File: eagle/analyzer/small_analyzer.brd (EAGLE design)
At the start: 55.5 x 30.5 mm, 22 parts, among them IC1 MCP604ST, IC2 TPS77301, IC3 MSP430FW42IP, U1 AD5933

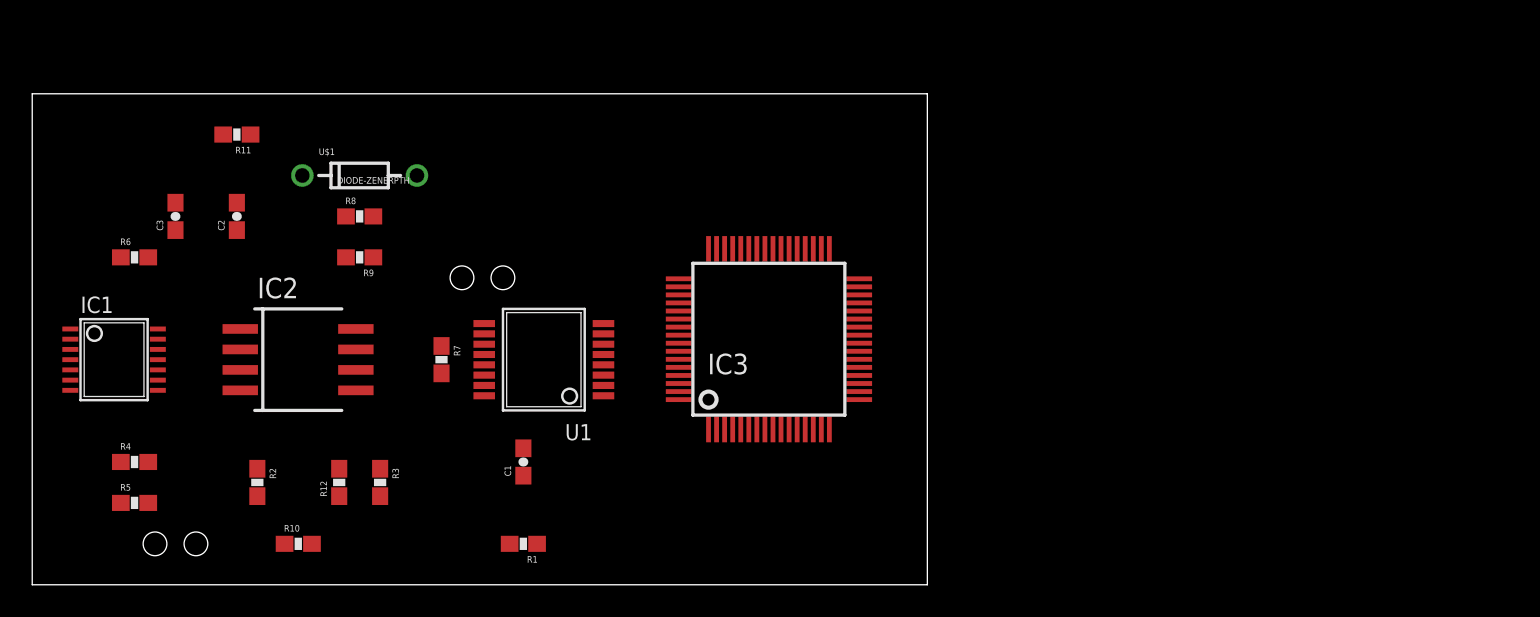
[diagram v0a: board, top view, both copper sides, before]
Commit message: added ground planes, expanded board, changed mcu to atmega328
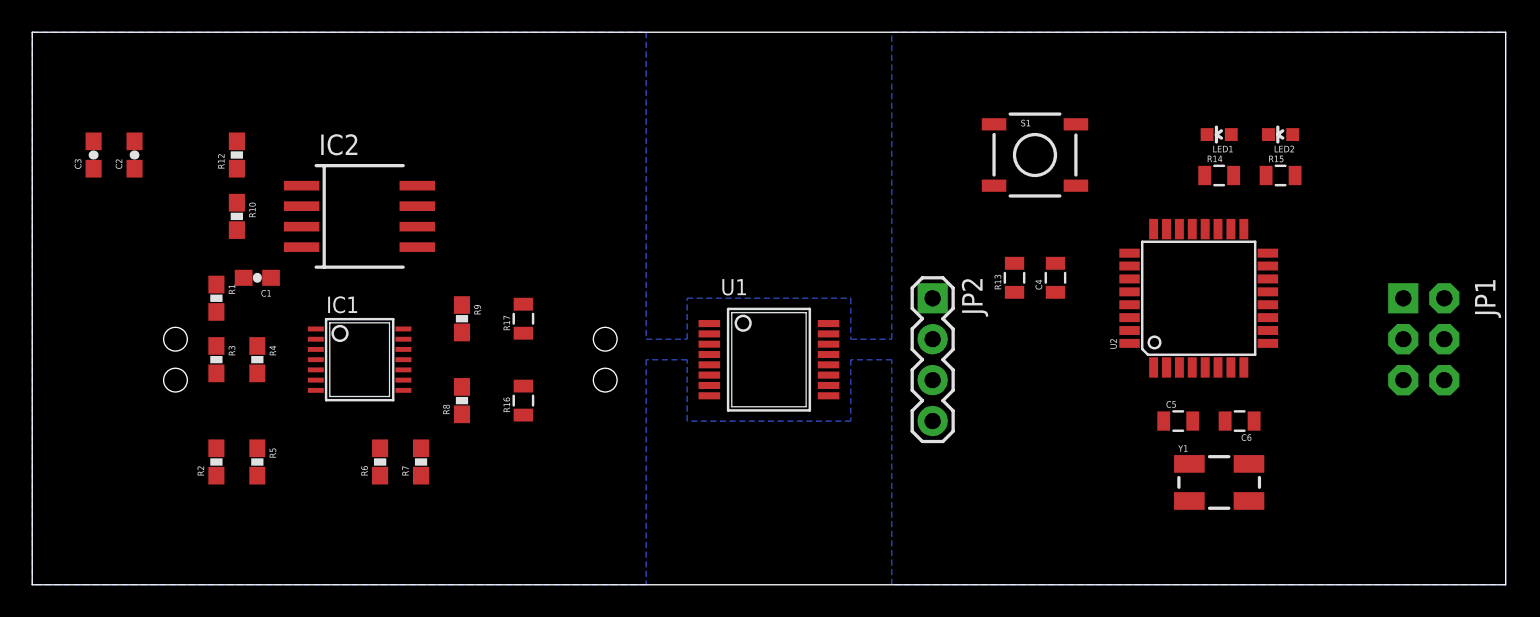
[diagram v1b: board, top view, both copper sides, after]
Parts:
- removed IC3: MSP430FW42IP, texas:SQFP-S-10X10-64
- removed R11: 10k, SparkFun-Passives:0603-RES
- removed U$1: DIODE-ZENERPTH, SparkFun-DiscreteSemi:DIODE-ZENER
- added C4: 0.1uF, SparkFun-Passives:0805
- added C5, C6: 22pF, SparkFun-Passives:0805
- added JP1: (no value), SparkFun-Connectors:2X3-NS
- added JP2: (no value), SparkFun-Connectors:1X04
- added LED1, LED2: (no value), SparkFun-LED:LED-0603
- added R13: 10k, SparkFun-Passives:0805
- added R14, R15: 4.7k, SparkFun-Passives:0805
- added R16, R17: 100k, SparkFun-Passives:0805
- added S1: (no value), SparkFun-Electromechanical:TACTILE_SWITCH_SMD
- added U2: ATMEGA328P, SparkFun-DigitalIC:TQFP32-08
- added Y1: (no value), SparkFun-FreqCtrl:CRYSTAL-SMD-5X3
- moved R1 24.4 mm to (11.4, 17.8), turned to 270 degrees
- moved R12 21.3 mm to (12.7, 26.7)
- moved R10 20.7 mm to (12.7, 22.9), turned to 270 degrees
- moved C1 20.1 mm to (14.0, 19.1), turned to 180 degrees
- moved R6 19.8 mm to (21.6, 7.62), turned to 90 degrees
- moved IC1 15.2 mm to (20.3, 14.0)
- moved U1 14.0 mm to (45.7, 14.0), turned to 270 degrees
- moved R8 13.1 mm to (26.7, 11.4), turned to 90 degrees
- moved LOAD 12.8 mm to (8.89, 15.2), turned to 270 degrees
- moved R3 12.7 mm to (11.4, 14.0)
- moved RFB 10.9 mm to (35.6, 12.7), turned to 90 degrees
- moved R4 9.92 mm to (14.0, 14.0), turned to 270 degrees
- moved IC2 9.67 mm to (20.3, 22.9)
- moved R5 8.03 mm to (14.0, 7.62), turned to 270 degrees
- moved C2 7.41 mm to (6.35, 26.7)
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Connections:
- removed net AVCC: IC3.64
- removed net AVSS: IC3.62
- removed net DVCC: IC3.1
- removed net DVSS: IC3.63
- new net CS: U2.14
- new net MISO: JP1.1, U2.16
- new net MOSI: JP1.4, U2.15
- new net N$10: LED2.A, R15.2
- new net N$11: C4.2, R13.1, S1.3, S1.4, U2.29
- new net N$12: LED1.A, R14.2
- new net N$15: IC1.12, R16.2, R17.1
- new net N$17: U2.23
- new net N$4: C5.2, U2.7, Y1.1
- new net N$9: C6.2, U2.8, Y1.3
- new net RST: C4.1, JP1.5
- new net SCK: JP1.3, R15.1, U2.17
- net GND: now also C5.1, C6.1, JP1.6, JP2.4, LED1.C, LED2.C, R16.1, S1.1, S1.2, U2.21, U2.3, U2.5; no longer U$1.P$2
- net MCLK: now also JP2.3
- net SCL: now also JP2.1, U2.28
- net SDA: now also JP2.2, U2.27
- net VCC: now also JP1.2, R13.2, R14.1, R17.2, U2.18, U2.20, U2.4, U2.6; no longer R11.2
- net VREF: now also IC1.13, IC1.14; no longer R11.1, U$1.P$1
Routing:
- added copper zone on layer 16, net GND
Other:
- board size 55.5 x 30.5 mm -> 91.4 x 34.3 mm

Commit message: updated
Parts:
- removed C3: 0.1uF, SparkFun-Passives:0603-CAP
- removed LOAD, RFB: M02POGO_PIN_HOLES_ONLY, SparkFun-Connectors:1X02_PP_HOLES_ONLY
- added C7: 10uF, SparkFun-Passives:0603-CAP
- added C8: 0.1uF, SparkFun-Passives:0603-CAP
- added IC3: TPS77350, texas:SOP-08
- added JP3: (no value), SparkFun-Connectors:1X04
- added JP4: (no value), SparkFun-Connectors:1X06_LOCK
- C2: value 10uF -> 0.1uF
- moved C2 36.3 mm to (35.6, 5.08), turned to 270 degrees
- moved JP2 13.0 mm to (53.3, 30.5)
- moved U1 11.7 mm to (43.2, 25.4)
- moved JP1 3.59 mm to (83.8, 17.8)
- moved C5 3.59 mm to (68.6, 12.7)
- moved C6 3.59 mm to (72.4, 12.7)
- moved U2 3.59 mm to (69.8, 20.3)
- moved C4 3.59 mm to (61.0, 21.6)
- moved R13 3.59 mm to (58.4, 21.6)
- moved S1 3.59 mm to (59.7, 29.2)
- moved R14 3.59 mm to (71.1, 27.9)
- moved R15 3.59 mm to (74.9, 27.9)
- moved Y1 3.59 mm to (71.1, 8.89)
- moved LED1 3.59 mm to (71.1, 30.5)
- moved LED2 3.59 mm to (74.9, 30.5)
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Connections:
- new net RXI: JP4.3, U2.30
- new net TXO: JP4.2, U2.31
- new net VBAT: C7.1, C8.1, IC3.2, JP4.4
- net +IN: now also JP3.3; no longer LOAD.2
- net -IN: now also JP3.4; no longer LOAD.1
- net GND: now also C7.2, C8.2, IC3.4, JP4.5, JP4.6; no longer C3.2
- net IOUT2: now also JP3.1; no longer RFB.1
- net RFB: now also JP3.2; no longer RFB.2
- net RST: now also JP4.1
- net VCC: now also IC3.7; no longer C3.1
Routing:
- net GND: track 0.00 -> 215.9 mm, vias 0 -> 8
- net VCC: track 0.00 -> 135.1 mm, vias 0 -> 7
- net +IN: track 0.00 -> 60.6 mm, vias 0 -> 4
- net VBAT: track 0.00 -> 32.3 mm, vias 0 -> 2
- net VIN: track 0.00 -> 32.2 mm, vias 0 -> 2
- net IOUT2: track 0.00 -> 31.0 mm, vias 0 -> 2
- net -IN: track 0.00 -> 26.9 mm
- net SCL: track 0.00 -> 24.0 mm, vias 0 -> 2
- net N$11: track 0.00 -> 23.7 mm, vias 0 -> 2
- net SDA: track 0.00 -> 22.7 mm, vias 0 -> 1
- net SCK: track 0.00 -> 18.1 mm
- net RXI: track 0.00 -> 17.8 mm, vias 0 -> 1
- net MCLK: track 0.00 -> 15.8 mm, vias 0 -> 1
- net N$3: track 0.00 -> 15.8 mm, vias 0 -> 2
- net TXO: track 0.00 -> 15.0 mm, vias 0 -> 2
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- removed copper zone on layer 16, net GND

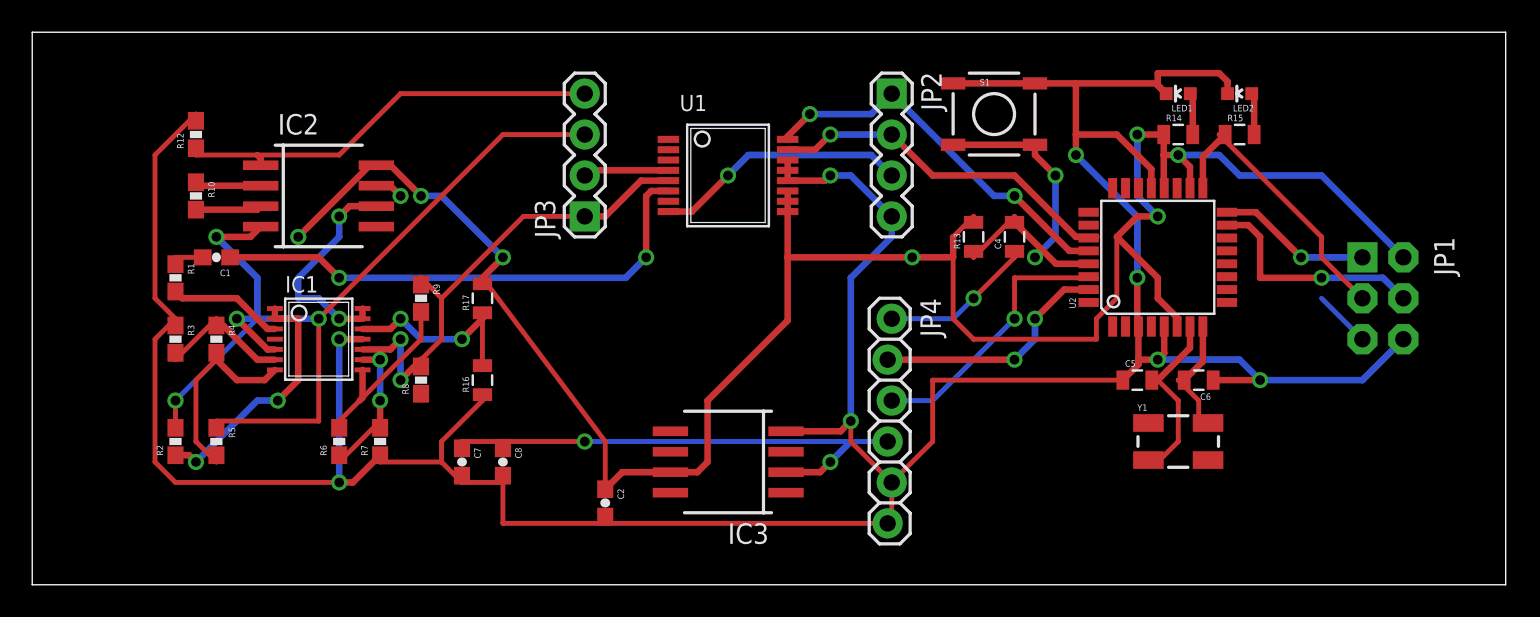
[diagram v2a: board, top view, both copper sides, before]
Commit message: all pins successfully routed
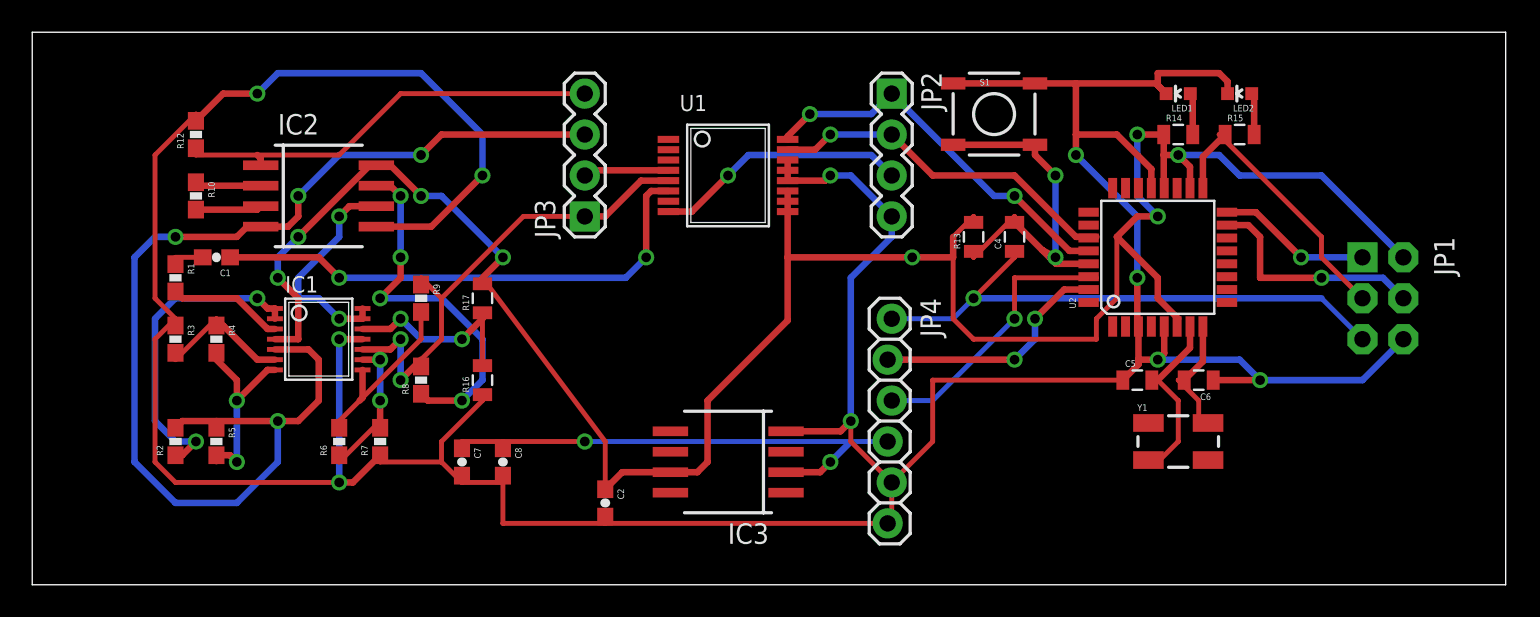
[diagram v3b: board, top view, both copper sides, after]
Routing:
- net GND: track 215.9 -> 247.0 mm, vias 8 -> 10
- net RST: track 13.2 -> 34.8 mm
- net VAMP: track 1.77 -> 23.1 mm, vias 1 -> 4
- net +IN: track 60.6 -> 73.6 mm
- net VCC: track 135.1 -> 144.0 mm, vias 7 -> 8
- net N$3: track 15.8 -> 19.9 mm
- net N$6: track 12.7 -> 11.9 mm, vias 0 -> 2

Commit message: local updates
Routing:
- added copper zone on layer 16, net GND
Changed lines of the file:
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@@
 <wire x1="69.85" y1="22.86" x2="68.58" y2="22.86" width="0.4064" layer="1"/>
 <wire x1="68.58" y1="22.86" x2="67.31" y2="21.59" width="0.4064" layer="1"/>
-<wire x1="71.05" y1="16.0274" x2="69.45" y2="16.0274" width="0" layer="19" extent="1-1"/>
 <wire x1="21.355" y1="26.035" x2="22.225" y2="26.035" width="0.4064" layer="1"/>
 <wire x1="22.225" y1="26.035" x2="24.13" y2="24.13" width="0.4064" layer="1"/>
@@
 <via x="29.21" y="20.32" extent="1-16" drill="0.6"/>
 <wire x1="29.21" y1="20.32" x2="27.94" y2="19.05" width="0.4064" layer="1"/>
-<wire x1="27.94" y1="19.05" x2="27.94" y2="18.68" width="0" layer="19" extent="1-16"/>
 <wire x1="21.355" y1="26.035" x2="20.955" y2="26.035" width="0.4064" layer="1"/>
 <wire x1="20.955" y1="26.035" x2="16.51" y2="21.59" width="0.4064" layer="1"/>
@@
 <wire x1="15.24" y1="19.05" x2="15.24" y2="20.32" width="0.4064" layer="16"/>
 <wire x1="15.24" y1="20.32" x2="16.51" y2="21.59" width="0.4064" layer="16"/>
+<wire x1="71.05" y1="16.0274" x2="69.45" y2="16.0274" width="0" layer="19" extent="1-1"/>
 </signal>
 <signal name="GND">
@@
 <wire x1="13.97" y1="30.48" x2="11.85" y2="30.48" width="0.4064" layer="1"/>
 <wire x1="11.85" y1="30.48" x2="10.16" y2="28.79" width="0.4064" layer="1"/>
+<polygon width="0.4064" layer="16">
+<vertex x="0" y="0"/>
+<vertex x="0" y="34.29"/>
+<vertex x="36.83" y="34.29"/>
+<vertex x="36.83" y="13.97"/>
+<vertex x="36.83" y="6.35"/>
+<vertex x="50.8" y="6.35"/>
+<vertex x="50.8" y="34.29"/>
+<vertex x="91.44" y="34.29"/>
+<vertex x="91.44" y="0"/>
+<vertex x="50.8" y="0"/>
+<vertex x="50.8" y="5.08"/>
+<vertex x="36.83" y="5.08"/>
+<vertex x="36.83" y="0"/>
+</polygon>
 </signal>
 <signal name="VIN">
@@
 <via x="22.86" y="12.7" extent="1-16" drill="0.6"/>
 <wire x1="22.86" y1="12.7" x2="24.13" y2="13.97" width="0.4064" layer="1"/>
-<wire x1="24.13" y1="13.97" x2="24.13" y2="13.55" width="0" layer="19" extent="1-16"/>
 </signal>
 <signal name="N$7">
@@
 <wire x1="11.43" y1="10.16" x2="9.31" y2="10.16" width="0.4064" layer="1"/>
 <wire x1="9.31" y1="10.16" x2="8.89" y2="9.74" width="0.4064" layer="1"/>
-<wire x1="11.43" y1="10.16" x2="12.7" y2="10.16" width="0" layer="19" extent="1-16"/>
-<wire x1="12.7" y1="10.16" x2="13.97" y2="11.43" width="0" layer="19" extent="1-16"/>
 <wire x1="15.0622" y1="14.605" x2="17.145" y2="14.605" width="0.4064" layer="1"/>
 <wire x1="17.145" y1="14.605" x2="17.78" y2="13.97" width="0.4064" layer="1"/>
@@
 <wire x1="69.85" y1="7.62" x2="69.27" y2="7.74" width="0.3048" layer="1"/>
 <wire x1="71.85" y1="16.0274" x2="71.85" y2="14.7" width="0.4064" layer="1"/>
-<wire x1="69.85" y1="13.97" x2="69.85" y2="13.07" width="0" layer="19" extent="1-16"/>
-<wire x1="69.85" y1="13.07" x2="69.48" y2="12.7" width="0" layer="19" extent="1-16"/>
 <wire x1="71.85" y1="14.7" x2="69.85" y2="12.7" width="0.4064" layer="1"/>
-<wire x1="69.85" y1="12.7" x2="69.48" y2="12.7" width="0" layer="19" extent="1-16"/>
 </signal>
 <signal name="N$9">
